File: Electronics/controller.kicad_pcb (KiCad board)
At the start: 2 copper layers, 100 x 100 mm, 124 parts, among them J301 UART, J501 Switches, J502 Motor Con, J503 Hall Sensor, Q201 IRLZ44N, Q202 IRLIZ44N, Q203 IRLZ44N, Q204 IRLIZ44N, Q205 IRLZ44N, Q206 IRLIZ44N, Q501 BC817, U201 74AHC08, U202 IR2101, U203 IR2101, U204 IR2101, U301 74HC86, U302 74AHC08, U401 R-78C5.0-1.0, U402 R-78C15-1.0, U501 ‎ACHS-7124-000E‎, U502 LM393, U503 74AHC08, U504 MCP6001-OT

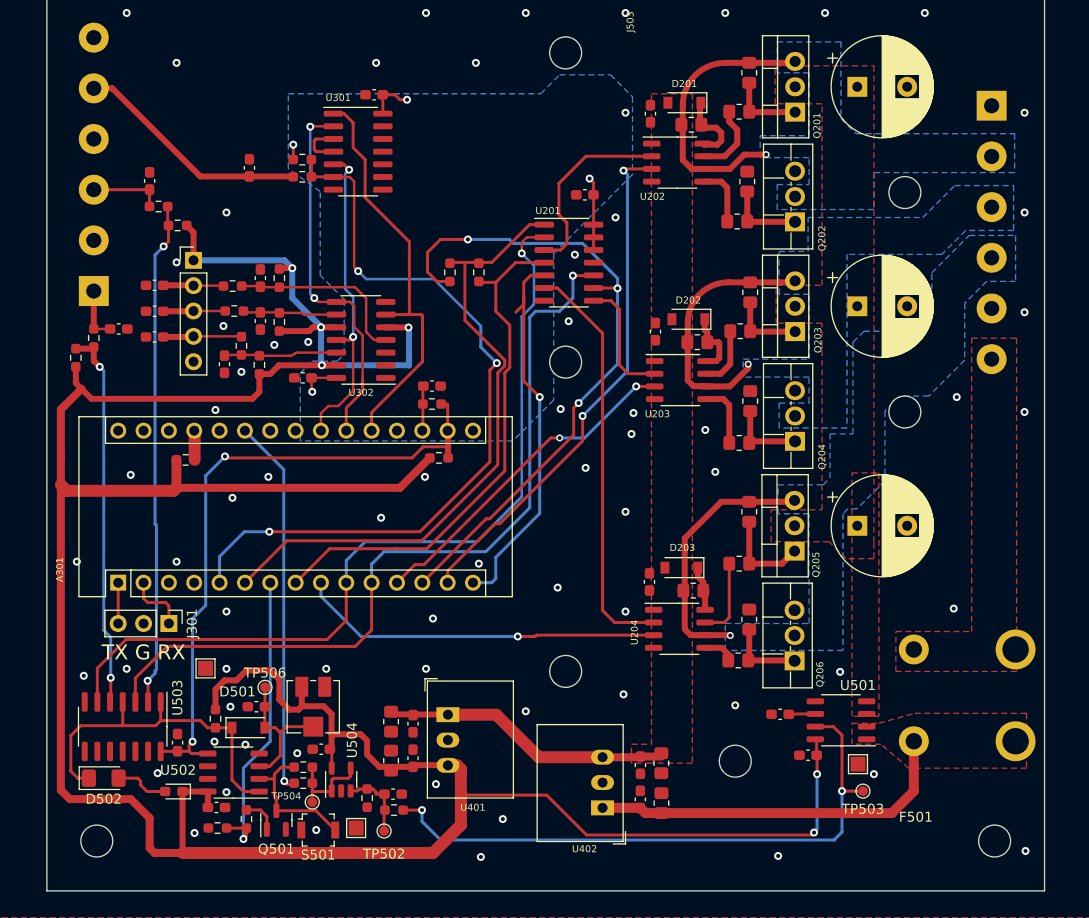
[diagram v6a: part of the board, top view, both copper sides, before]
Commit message: Chaned 74AHC08 footprint to ssop-14
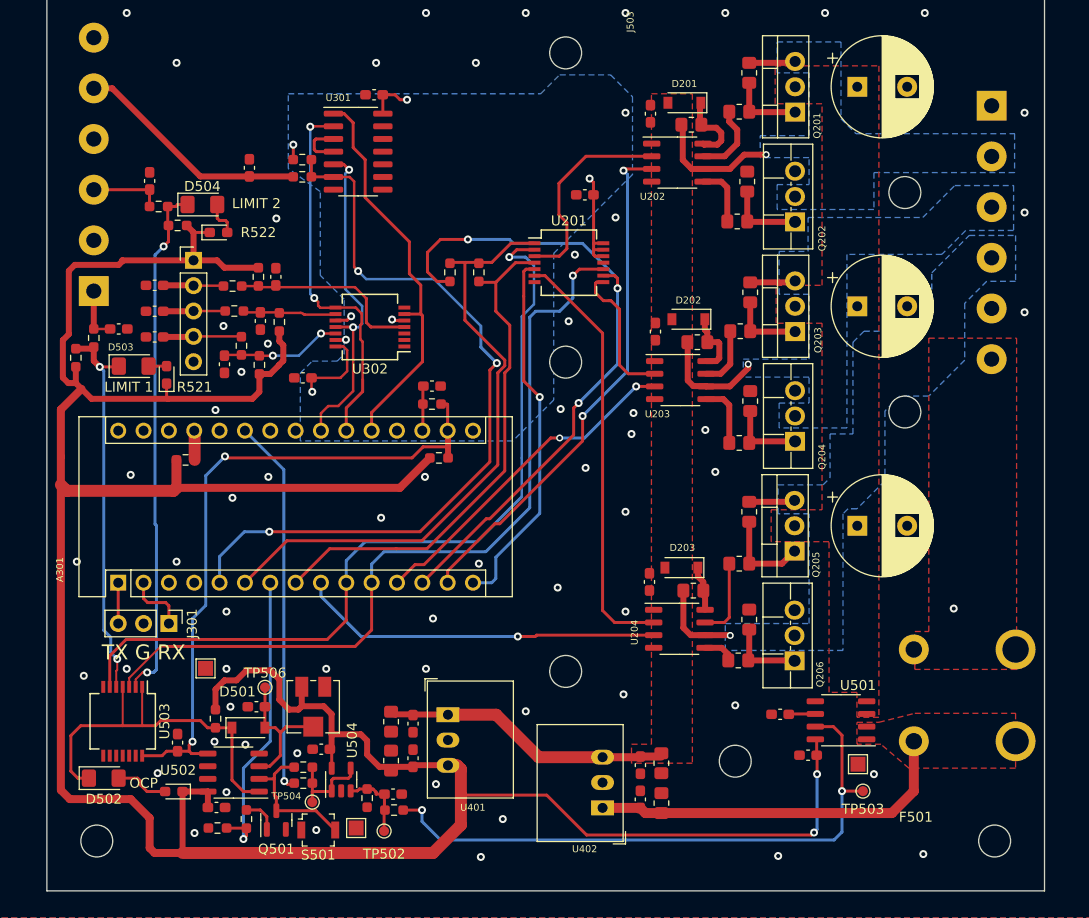
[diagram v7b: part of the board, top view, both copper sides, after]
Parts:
- added D503: LED, LED_SMD:LED_1206_3216Metric_Pad1.42x1.75mm_HandSolder, F.Cu at (85.7, 90.4)
- added D504: LED, LED_SMD:LED_1206_3216Metric_Pad1.42x1.75mm_HandSolder, F.Cu at (92.6, 74.2)
- added R521: 1k, LED_SMD:LED_0603_1608Metric_Pad1.05x0.95mm_HandSolder, F.Cu at (89.0, 91.3)
- added R522: 1k, LED_SMD:LED_0603_1608Metric_Pad1.05x0.95mm_HandSolder, F.Cu at (94.2, 77.0)
- U201, U302, U503: footprint Package_SO:SO-14_3.9x8.65mm_P1.27mm -> Package_SO:SSOP-14_5.3x6.2mm_P0.65mm
- moved R512 2.10 mm to (98.2, 81.5)
- moved U302 1.57 mm to (109.4, 86.5)
- moved C509 1.56 mm to (100.0, 81.5)
- moved U503 0.54 mm to (84.6, 126.0)
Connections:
- U302 pad 10: VDD -> +3V3
- U302 pad 13: VDD -> +3V3
- U302 pad 5: VDD -> +3V3
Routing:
- net +3V3: track 82.1 -> 96.4 mm, vias 6 -> 9
- net /Connectors/MOTOR C: track 26.5 -> 13.4 mm
- net /Connectors/MOTOR POS: track 28.4 -> 17.2 mm
- net /Connectors/MOTOR NEG: track 26.2 -> 15.9 mm
- net VDD: track 309.0 -> 299.2 mm, vias 6 -> 2
- net Net-(D504-Pad2): track 0.00 -> 3.57 mm
- net Net-(D501-Pad1): track 35.4 -> 39.0 mm
- net /Hbridge/C LIMIT: track 38.9 -> 36.9 mm
- net Net-(U201-Pad8): track 12.4 -> 14.4 mm
- net /Connectors/LIMIT 2: track 50.4 -> 52.3 mm
- net Net-(D503-Pad2): track 0.00 -> 1.81 mm
- net /Hbridge/HIN A: track 63.5 -> 61.8 mm
- net /Connectors/Limit 1: track 85.5 -> 83.9 mm
- net Net-(U201-Pad3): track 19.3 -> 20.9 mm
- net Net-(U201-Pad6): track 41.1 -> 42.6 mm
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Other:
- board text added: "LIMIT 1"
- board text added: "LIMIT 2"
- board text added: "OCP"

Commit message: Layout improvements
Signed-off-by: Aki Kuusela <git@findersee.fi>
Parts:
- added J302: I2C, Connector_PinHeader_2.54mm:PinHeader_1x04_P2.54mm_Vertical, F.Cu at (104.5, 93.1)
- U201: value 74AHC08 -> 74LS08; footprint Package_SO:SSOP-14_5.3x6.2mm_P0.65mm -> Package_SO:SO-14_3.9x8.65mm_P1.27mm
- moved C507 5.30 mm to (100.0, 89.2), turned to 90 degrees
- moved R511 1.91 mm to (98.4, 85.8)
- moved C508 1.60 mm to (100.0, 85.8)
- moved C302 1.34 mm to (103.3, 90.4)
- moved C201 1.27 mm to (130.9, 74.5)
- moved R509 1.18 mm to (95.6, 87.6), turned to 0 degrees
- moved R510 1.08 mm to (98.4, 89.2), turned to -90 degrees
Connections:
- A301 pad 23: unconnected-(A301-Pad23) -> Net-(A301-Pad23)
- A301 pad 24: unconnected-(A301-Pad24) -> Net-(A301-Pad24)
- A301 pad 26: unconnected-(A301-Pad26) -> /Connectors/Over Current
- U503 pad 11: unconnected-(U503-Pad11) -> /Connectors/Over Current
- U503 pad 12: GND -> Net-(D501-Pad1)
- U503 pad 13: GND -> +3V3
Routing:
- net /Connectors/Over Current: track 0.00 -> 38.0 mm, vias 0 -> 1
- net /MCU/HALL C OUT: track 33.2 -> 38.3 mm
- net VDD: track 299.2 -> 294.3 mm
- net Net-(D501-Pad1): track 39.0 -> 43.6 mm
- net /Hbridge/HIN A: track 61.8 -> 66.1 mm
- net Net-(A301-Pad24): track 0.00 -> 3.81 mm
- net Net-(A301-Pad23): track 0.00 -> 3.81 mm
- net Net-(U201-Pad3): track 20.9 -> 17.5 mm
- net /Hbridge/C LIMIT: track 36.9 -> 39.7 mm
- net /Connectors/Limit 1: track 83.9 -> 86.5 mm
- net /Connectors/Button: track 78.1 -> 80.6 mm, vias 3 -> 2
- net /Hbridge/LIN B: track 34.0 -> 36.0 mm
- net Net-(C504-Pad1): track 7.68 -> 5.93 mm
- net /Hbridge/LIN A: track 52.1 -> 53.8 mm
- net /Connectors/Limit 2: track 81.8 -> 80.2 mm
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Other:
- board text added: "0.1600 mm / 0.1600 mm"
- board text added: "100.1000 mm x 100.1000 mm"
- board text added: "GND Motor A Motor B Motor C NC PWR MAX 40V"
- board text removed: "0.2000 mm / 0.0000 mm"
- board text removed: "100.1000 mm x 75.1000 mm"
- board text removed: "GND Motor A Motor B Motor C NC Power MAX 40V"
